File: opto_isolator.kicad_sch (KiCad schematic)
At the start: 6 parts, among them IC4 TLP2366_TPL,E, J9 Conn_Coaxial

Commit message: First finished version. Still need to check some footprint for critical parts and also refine the part numbers before order
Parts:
- J9: footprint Connector_Coaxial:SMA_Amphenol_132134-10_Vertical -> Connector_Coaxial:SMA_Amphenol_132134_Vertical

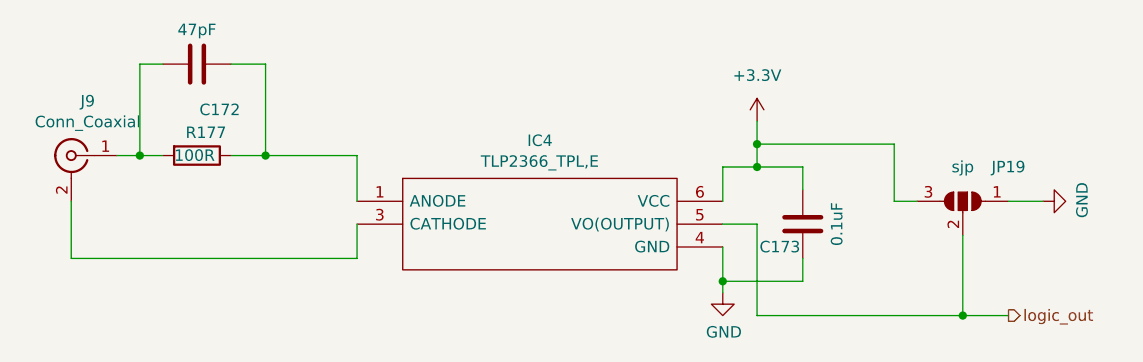
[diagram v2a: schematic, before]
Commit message: Version 1.0 submitted to JLCPCB
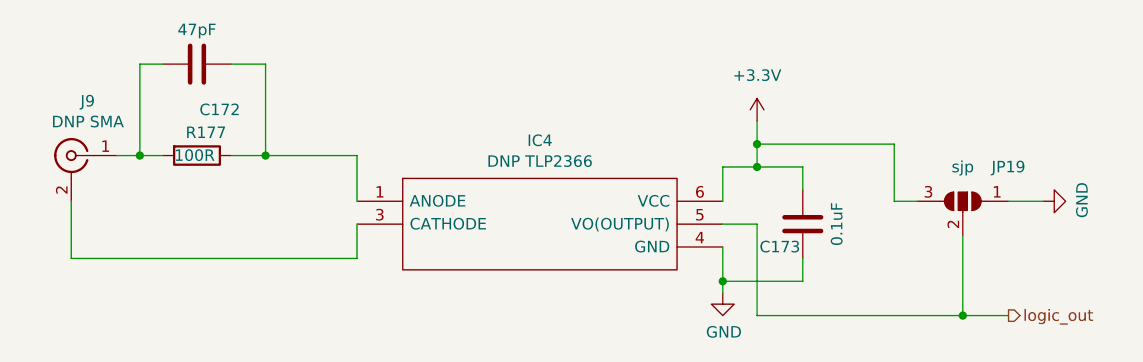
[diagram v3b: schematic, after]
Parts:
- IC4: value TLP2366_TPL,E -> DNP TLP2366
- J9: value Conn_Coaxial -> DNP SMA
